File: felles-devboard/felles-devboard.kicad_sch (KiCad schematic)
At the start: 25 parts, among them Q1 STANDARD_140356145200, U1 TPS26400PWP, U2 173950336, U3 TCAN332G, U4 BME280, U5 WE-TVS-824015043

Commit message: Moved some stuff
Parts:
- removed U3: TCAN332G, Package_TO_SOT_SMD:TSOT-23-8, symbol Interface_CAN_LIN:TCAN332G
- added IC1: TCAN3413DR, SOIC127P600X175-8N, symbol Samacsys:TCAN3413DR
- C10: value 100n -> 1u
- R1: value R -> 470k
- R2: value R -> 15k
- R3: value R -> 30k
- R4: value R -> 24k9
- R5: value R -> 10k
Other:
- moved on the sheet: Q1, R6, R7

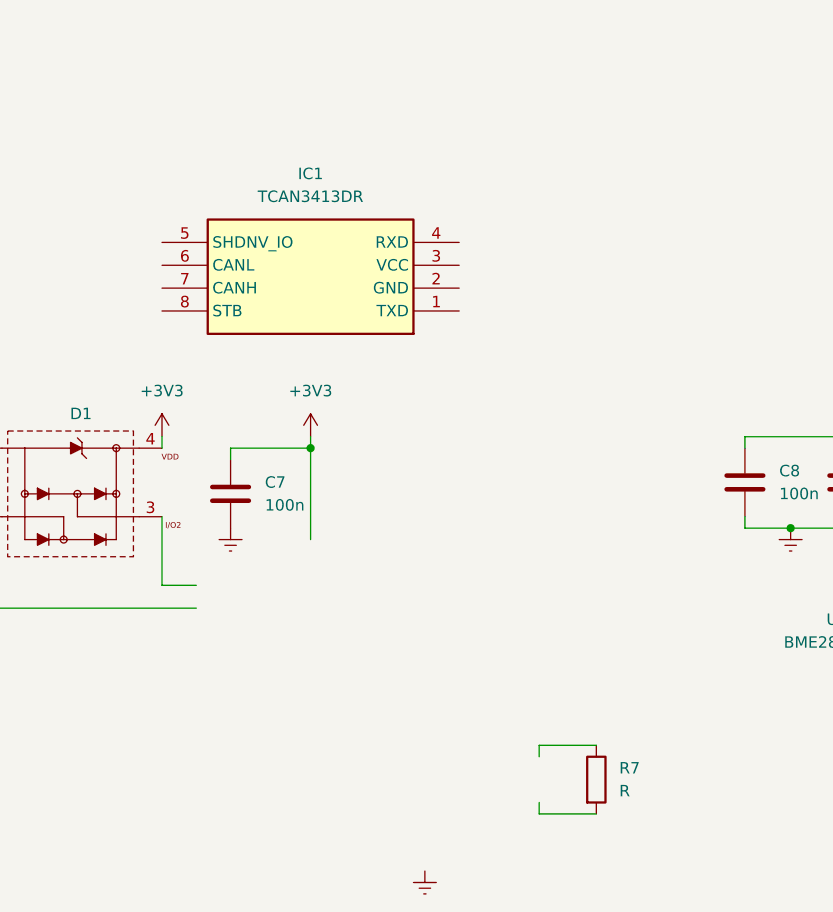
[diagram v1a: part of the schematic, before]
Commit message: Generert PDF av skjematikken
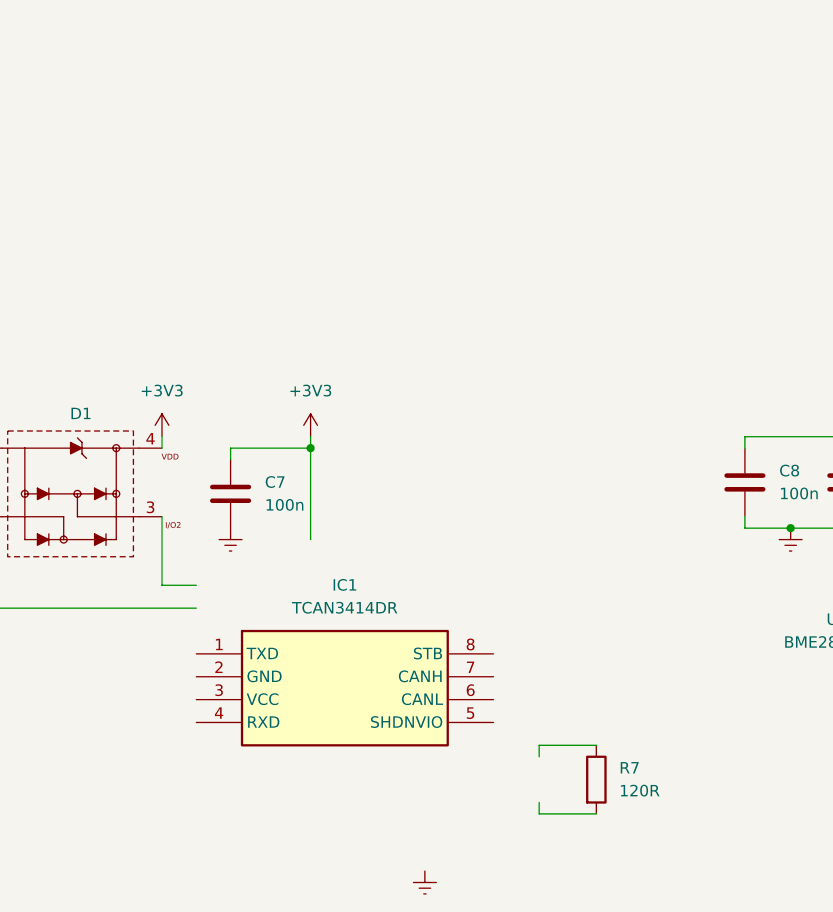
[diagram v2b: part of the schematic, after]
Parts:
- removed IC1: TCAN3413DR, SOIC127P600X175-8N, symbol Samacsys:TCAN3413DR
- added IC1: TCAN3414DR, Samacsys:SOIC127P600X175-8N, symbol Samacsys:TCAN3414DR
- R7: value R -> 120R
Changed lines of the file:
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@@
 	)
 	(symbol
-		(lib_id "Samacsys:TCAN3413DR")
-		(at 163.83 93.98 180)
-		(unit 1)
-		(body_style 1)
-		(exclude_from_sim no)
-		(in_bom yes)
-		(on_board yes)
-		(in_pos_files yes)
-		(dnp no)
-		(fields_autoplaced yes)
-		(property "Reference" "IC1"
-			(at 147.32 78.74 0)
-			(show_name no)
-			(do_not_autoplace no)
-			(effects
-				(font
-					(size 1.27 1.27)
-				)
-			)
-		)
-		(property "Value" "TCAN3413DR"
-			(at 147.32 81.28 0)
-			(show_name no)
-			(do_not_autoplace no)
-			(effects
-				(font
-					(size 1.27 1.27)
-				)
-			)
-		)
-		(property "Footprint" "SOIC127P600X175-8N"
-			(at 147.32 116.84 0)
-			(hide yes)
-			(show_name yes)
-			(do_not_autoplace no)
-			(effects
-				(font
-					(size 1.27 1.27)
-				)
-			)
-		)
-		(property "Datasheet" "https://www.ti.com/lit/ds/symlink/tcan3413.pdf?ts=1704463166829&ref_url=https%253A%252F%252Fwww.ti.com%252Fproduct%252Fde-de%252FTCAN3413"
-			(at 147.32 114.3 0)
-			(hide yes)
-			(show_name yes)
-			(do_not_autoplace no)
-			(effects
-				(font
-					(size 1.27 1.27)
-				)
-			)
-		)
-		(property "Description" "1/1 Transceiver Half CANbus 8-SOIC"
-			(at 147.32 111.76 0)
-			(hide yes)
-			(show_name yes)
-			(do_not_autoplace no)
-			(effects
-				(font
-					(size 1.27 1.27)
-				)
-			)
-		)
-		(property "Height" "1.75"
-			(at 147.32 109.22 0)
-			(hide yes)
-			(show_name yes)
-			(do_not_autoplace no)
-			(effects
-				(font
-					(size 1.27 1.27)
-				)
-			)
-		)
-		(property "Mouser Part Number" "595-TCAN3413DR"
-			(at 147.32 106.68 0)
-			(hide yes)
-			(show_name yes)
-			(do_not_autoplace no)
-			(effects
-				(font
-					(size 1.27 1.27)
-				)
-			)
-		)
-		(property "Mouser Price/Stock" "https://www.mouser.co.uk/ProductDetail/Texas-Instruments/TCAN3413DR?qs=mELouGlnn3eIMT2B6sccyw%3D%3D"
-			(at 147.32 104.14 0)
-			(hide yes)
-			(show_name yes)
-			(do_not_autoplace no)
-			(effects
-				(font
-					(size 1.27 1.27)
-				)
-			)
-		)
-		(property "Manufacturer_Name" "Texas Instruments"
-			(at 147.32 101.6 0)
-			(hide yes)
-			(show_name yes)
-			(do_not_autoplace no)
-			(effects
-				(font
-					(size 1.27 1.27)
-				)
-			)
-		)
-		(property "Manufacturer_Part_Number" "TCAN3413DR"
-			(at 147.32 99.06 0)
-			(hide yes)
-			(show_name yes)
-			(do_not_autoplace no)
-			(effects
-				(font
-					(size 1.27 1.27)
-				)
-			)
-		)
-		(pin "2"
-		)
-		(pin "6"
-		)
-		(pin "5"
-		)
-		(pin "7"
-		)
-		(pin "1"
-		)
-		(pin "8"
-		)
-		(pin "3"
-		)
-		(pin "4"
-		)
-		(instances
-			(project "felles-devboard"
-				(path "/756ec426-2cce-4562-95fb-d349ef78b381"
-					(reference "IC1")
-					(unit 1)
-				)
-			)
-		)
-	)
-	(symbol
 		(lib_id "Device:R")
 		(at 179.07 146.05 0)
@@
 			)
 		)
-		(property "Value" "R"
+		(property "Value" "120R"
 			(at 181.61 147.3199 0)
 			(show_name no)
@@
 					(unit 1)
 				)
+			)
+		)
+	)
+	(symbol
+		(lib_id "Samacsys:TCAN3414DR")
+		(at 134.62 132.08 0)
+		(unit 1)
+		(body_style 1)
+		(exclude_from_sim no)
+		(in_bom yes)
+		(on_board yes)
+		(in_pos_files yes)
+		(dnp no)
+		(fields_autoplaced yes)
+		(property "Reference" "IC1"
+			(at 151.13 124.46 0)
+			(show_name no)
+			(do_not_autoplace no)
+			(effects
+				(font
+					(size 1.27 1.27)
+				)
+			)
+		)
+		(property "Value" "TCAN3414DR"
+			(at 151.13 127 0)
+			(show_name no)
+			(do_not_autoplace no)
+			(effects
+				(font
+					(size 1.27 1.27)
+				)
+			)
+		)
+		(property "Footprint" "Samacsys:SOIC127P600X175-8N"
+			(at 151.13 109.22 0)
+			(hide yes)
+			(show_name yes)
+			(do_not_autoplace no)
+			(effects
+				(font
+					(size 1.27 1.27)
+				)
+			)
+		)
+		(property "Datasheet" "https://www.ti.com/lit/ds/symlink/tcan3414.pdf?ts=1713723144569&ref_url=https%253A%252F%252Fwww.mouser.ch%252F"
+			(at 151.13 111.76 0)
+			(hide yes)
+			(show_name yes)
+			(do_not_autoplace no)
+			(effects
+				(font
+					(size 1.27 1.27)
+				)
+			)
+		)
+		(property "Description" "3.3-V CAN FD transceiver with shut-down and standby mode"
+			(at 151.13 114.3 0)
+			(hide yes)
+			(show_name yes)
+			(do_not_autoplace no)
+			(effects
+				(font
+					(size 1.27 1.27)
+				)
+			)
+		)
+		(property "Height" "1.75"
+			(at 151.13 116.84 0)
+			(hide yes)
+			(show_name yes)
+			(do_not_autoplace no)
+			(effects
+				(font
+					(size 1.27 1.27)
+				)
+			)
+		)
+		(property "Mouser Part Number" "595-TCAN3414DR"
+			(at 151.13 119.38 0)
+			(hide yes)
+			(show_name yes)
+			(do_not_autoplace no)
+			(effects
+				(font
+					(size 1.27 1.27)
+				)
+			)
+		)
+		(property "Mouser Price/Stock" "https://www.mouser.co.uk/ProductDetail/Texas-Instruments/TCAN3414DR?qs=mELouGlnn3egF2AojRJddw%3D%3D"
+			(at 151.13 121.92 0)
+			(hide yes)
+			(show_name yes)
+			(do_not_autoplace no)
+			(effects
+				(font
+					(size 1.27 1.27)
+				)
+			)
+		)
+		(property "Manufacturer_Name" "Texas Instruments"
+			(at 151.13 124.46 0)
+			(hide yes)
+			(show_name yes)
+			(do_not_autoplace no)
+			(effects
+				(font
+					(size 1.27 1.27)
+				)
+			)
+		)
+		(property "Manufacturer_Part_Number" "TCAN3414DR"
+			(at 151.13 127 0)
+			(hide yes)
+			(show_name yes)
+			(do_not_autoplace no)
+			(effects
+				(font
+					(size 1.27 1.27)
+				)
+			)
+		)
+		(pin "6"
+		)
+		(pin "3"
+		)
+		(pin "1"
+		)
+		(pin "2"
+		)
+		(pin "4"
+		)
+		(pin "5"
+		)
+		(pin "7"
+		)
+		(pin "8"
+		)
+		(instances
+			(project "felles-devboard"
+				(path "/756ec426-2cce-4562-95fb-d349ef78b381"
+					(reference "IC1")
+					(unit 1)
+				)
